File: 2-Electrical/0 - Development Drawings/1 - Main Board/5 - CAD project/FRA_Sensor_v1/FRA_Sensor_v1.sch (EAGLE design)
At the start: 213 parts, among them IC1 CP2101, IC2 ADS1115IDGSR, IC3 P82B715DR, IC4 ADS1115IDGSR, IC5 ADS1115IDGSR, IC8 PCA9555PW, IC9 LDK320ADU50R, J2 ETH_CONN, J3 PJ-059A, J4 DNI, J5 WM9734TR-ND, J8 1140084168, J9 4pin, Q10 FDN306P, Q11 FDN306P, Q12 FDN306P, Q13 FDN306P, Q14 FDN306P, Q15 FDN306P, Q2 FDN306P, Q3 Si2300DS, Q5 FDN306P, Q6 FDN306P, Q7 DNI, Q8 FDN306P, Q9 FDN306P, T1 BC847, T2 BC847, U1 PCA9509DP, U2 ESP-WROOM-32, X1 TB001-500-02BE, Y3 DNI

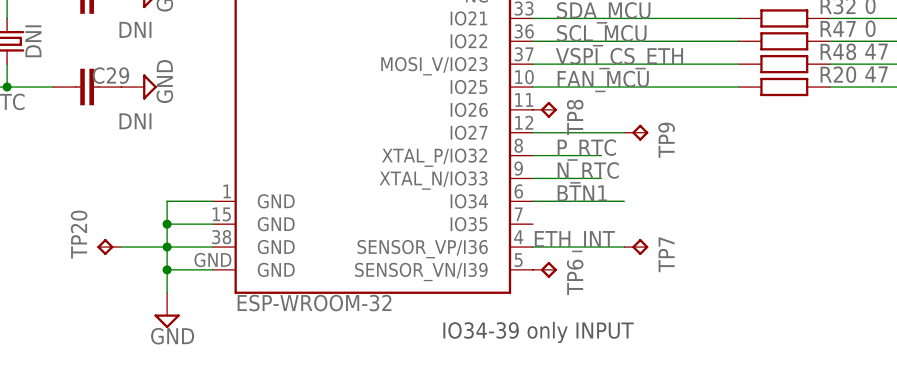
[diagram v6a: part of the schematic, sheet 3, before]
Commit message: edited ESP32 footprint
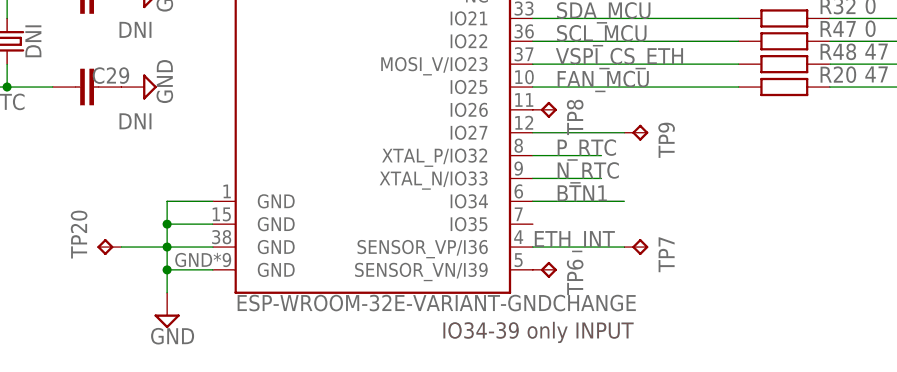
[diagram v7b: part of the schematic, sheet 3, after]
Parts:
- U2: value ESP-WROOM-32 -> ESP-WROOM-32E-VARIANT-GNDCHANGE; device SparkFun-RF:ESP-WROOM-32 -> FRA_eagle_lib:ESP-WROOM-32E-VARIANT-GNDCHANGE
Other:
- moved on the sheet: U2
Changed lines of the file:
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@@
 <?xml version="1.0" encoding="utf-8"?>
 <!DOCTYPE eagle SYSTEM "eagle.dtd">
-<eagle version="9.5.2">
+<eagle version="9.6.2">
 <drawing>
 <settings>
@@
 <grid distance="0.1" unitdist="inch" unit="inch" style="lines" multiple="1" display="no" altdistance="0.01" altunitdist="inch" altunit="inch"/>
 <layers>
-<layer number="1" name="Top" color="4" fill="1" visible="no" active="no"/>
-<layer number="2" name="Route2" color="1" fill="3" visible="no" active="no"/>
-<layer number="3" name="Route3" color="4" fill="3" visible="no" active="no"/>
-<layer number="4" name="Route4" color="1" fill="4" visible="no" active="no"/>
-<layer number="5" name="Route5" color="4" fill="4" visible="no" active="no"/>
-<layer number="6" name="Route6" color="1" fill="8" visible="no" active="no"/>
-<layer number="7" name="Route7" color="4" fill="8" visible="no" active="no"/>
-<layer number="8" name="Route8" color="1" fill="2" visible="no" active="no"/>
-<layer number="9" name="Route9" color="4" fill="2" visible="no" active="no"/>
-<layer number="10" name="Route10" color="1" fill="7" visible="no" active="no"/>
-<layer number="11" name="Route11" color="4" fill="7" visible="no" active="no"/>
-<layer number="12" name="Route12" color="1" fill="5" visible="no" active="no"/>
-<layer number="13" name="Route13" color="4" fill="5" visible="no" active="no"/>
-<layer number="14" name="Route14" color="1" fill="6" visible="no" active="no"/>
-<layer number="15" name="Route15" color="4" fill="6" visible="no" active="no"/>
-<layer number="16" name="Bottom" color="1" fill="1" visible="no" active="no"/>
-<layer number="17" name="Pads" color="2" fill="1" visible="no" active="no"/>
-<layer number="18" name="Vias" color="2" fill="1" visible="no" active="no"/>
-<layer number="19" name="Unrouted" color="6" fill="1" visible="no" active="no"/>
-<layer number="20" name="Dimension" color="15" fill="1" visible="no" active="no"/>
-<layer number="21" name="tPlace" color="7" fill="1" visible="no" active="no"/>
-<layer number="22" name="bPlace" color="7" fill="1" visible="no" active="no"/>
-<layer number="23" name="tOrigins" color="15" fill="1" visible="no" active="no"/>
-<layer number="24" name="bOrigins" color="15" fill="1" visible="no" active="no"/>
-<layer number="25" name="tNames" color="58" fill="1" visible="no" active="no"/>
-<layer number="26" name="bNames" color="7" fill="1" visible="no" active="no"/>
-<layer number="27" name="tValues" color="7" fill="1" visible="no" active="no"/>
-<layer number="28" name="bValues" color="7" fill="1" visible="no" active="no"/>
+<layer number="1" name="Top" color="4" fill="1" visible="yes" active="no"/>
+<layer number="2" name="Route2" color="1" fill="3" visible="yes" active="no"/>
+<layer number="3" name="Route3" color="4" fill="3" visible="yes" active="no"/>
+<layer number="4" name="Route4" color="1" fill="4" visible="yes" active="no"/>
+<layer number="5" name="Route5" color="4" fill="4" visible="yes" active="no"/>
+<layer number="6" name="Route6" color="1" fill="8" visible="yes" active="no"/>
+<layer number="7" name="Route7" color="4" fill="8" visible="yes" active="no"/>
+<layer number="8" name="Route8" color="1" fill="2" visible="yes" active="no"/>
+<layer number="9" name="Route9" color="4" fill="2" visible="yes" active="no"/>
+<layer number="10" name="Route10" color="1" fill="7" visible="yes" active="no"/>
+<layer number="11" name="Route11" color="4" fill="7" visible="yes" active="no"/>
+<layer number="12" name="Route12" color="1" fill="5" visible="yes" active="no"/>
+<layer number="13" name="Route13" color="4" fill="5" visible="yes" active="no"/>
+<layer number="14" name="Route14" color="1" fill="6" visible="yes" active="no"/>
+<layer number="15" name="Route15" color="4" fill="6" visible="yes" active="no"/>
+<layer number="16" name="Bottom" color="1" fill="1" visible="yes" active="no"/>
+<layer number="17" name="Pads" color="2" fill="1" visible="yes" active="no"/>
+<layer number="18" name="Vias" color="2" fill="1" visible="yes" active="no"/>
+<layer number="19" name="Unrouted" color="6" fill="1" visible="yes" active="no"/>
+<layer number="20" name="Dimension" color="15" fill="1" visible="yes" active="no"/>
+<layer number="21" name="tPlace" color="7" fill="1" visible="yes" active="no"/>
+<layer number="22" name="bPlace" color="7" fill="1" visible="yes" active="no"/>
+<layer number="23" name="tOrigins" color="15" fill="1" visible="yes" active="no"/>
+<layer number="24" name="bOrigins" color="15" fill="1" visible="yes" active="no"/>
+<layer number="25" name="tNames" color="58" fill="1" visible="yes" active="no"/>
+<layer number="26" name="bNames" color="7" fill="1" visible="yes" active="no"/>
+<layer number="27" name="tValues" color="7" fill="1" visible="yes" active="no"/>
+<layer number="28" name="bValues" color="7" fill="1" visible="yes" active="no"/>
 <layer number="29" name="tStop" color="7" fill="3" visible="no" active="no"/>
 <layer number="30" name="bStop" color="7" fill="6" visible="no" active="no"/>
@@
 <layer number="35" name="tGlue" color="7" fill="4" visible="no" active="no"/>
 <layer number="36" name="bGlue" color="7" fill="5" visible="no" active="no"/>
-<layer number="37" name="tTest" color="7" fill="1" visible="no" active="no"/>
-<layer number="38" name="bTest" color="7" fill="1" visible="no" active="no"/>
+<layer number="37" name="tTest" color="7" fill="1" visible="yes" active="no"/>
+<layer number="38" name="bTest" color="7" fill="1" visible="yes" active="no"/>
 <layer number="39" name="tKeepout" color="4" fill="11" visible="no" active="no"/>
 <layer number="40" name="bKeepout" color="1" fill="11" visible="no" active="no"/>
@@
 <layer number="44" name="Drills" color="7" fill="1" visible="no" active="no"/>
 <layer number="45" name="Holes" color="7" fill="1" visible="no" active="no"/>
-<layer number="46" name="Milling" color="3" fill="1" visible="no" active="no"/>
-<layer number="47" name="Measures" color="7" fill="1" visible="no" active="no"/>
-<layer number="48" name="Document" color="7" fill="1" visible="no" active="no"/>
-<layer number="49" name="Reference" color="7" fill="1" visible="no" active="no"/>
-<layer number="50" name="dxf" color="7" fill="1" visible="no" active="no"/>
-<layer number="51" name="tDocu" color="7" fill="1" visible="no" active="no"/>
-<layer number="52" name="bDocu" color="7" fill="1" visible="no" active="no"/>
-<layer number="53" name="tGND_GNDA" color="7" fill="9" visible="no" active="no"/>
-<layer number="54" name="bGND_GNDA" color="1" fill="9" visible="no" active="no"/>
-<layer number="56" name="wert" color="7" fill="1" visible="no" active="no"/>
-<layer number="57" name="tCAD" color="7" fill="1" visible="no" active="no"/>
-<layer number="59" name="tCarbon" color="7" fill="1" visible="no" active="no"/>
-<layer number="60" name="bCarbon" color="7" fill="1" visible="no" active="no"/>
+<layer number="46" name="Milling" color="3" fill="1" visible="yes" active="no"/>
+<layer number="47" name="Measures" color="7" fill="1" visible="yes" active="no"/>
+<layer number="48" name="Document" color="7" fill="1" visible="yes" active="no"/>
+<layer number="49" name="Reference" color="7" fill="1" visible="yes" active="no"/>
+<layer number="50" name="dxf" color="7" fill="1" visible="yes" active="no"/>
+<layer number="51" name="tDocu" color="7" fill="1" visible="yes" active="no"/>
+<layer number="52" name="bDocu" color="7" fill="1" visible="yes" active="no"/>
+<layer number="53" name="tGND_GNDA" color="7" fill="9" visible="yes" active="no"/>
+<layer number="54" name="bGND_GNDA" color="1" fill="9" visible="yes" active="no"/>
+<layer number="56" name="wert" color="7" fill="1" visible="yes" active="no"/>
+<layer number="57" name="tCAD" color="7" fill="1" visible="yes" active="no"/>
+<layer number="59" name="tCarbon" color="7" fill="1" visible="yes" active="no"/>
+<layer number="60" name="bCarbon" color="7" fill="1" visible="yes" active="no"/>
 <layer number="88" name="SimResults" color="9" fill="1" visible="yes" active="yes"/>
 <layer number="89" name="SimProbes" color="9" fill="1" visible="yes" active="yes"/>
@@
 <attributes>
 <attribute name="CNAME" value="FRA Sensor Unit"/>
-<attribute name="CREVISION" value="05"/>
+<attribute name="CREVISION" value="06"/>
 </attributes>
 <variantdefs>
@@
 </classes>
 <parts>
-<part name="U2" library="SparkFun-RF" deviceset="ESP-WROOM-32" device="">
+<part name="U2" library="FRA_eagle_lib" deviceset="ESP-WROOM-32" device="E-VARIANT-GNDCHANGE">
 <attribute name="PARTNO" value="ESP32-WROOM-32"/>
 </part>
